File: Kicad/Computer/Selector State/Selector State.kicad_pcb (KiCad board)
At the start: 2 copper layers, 61 x 61 mm, 72 parts, among them IC1 FAN2558S38X, IC10 74LVC257AD,118, IC11 74LVC257AD,118, IC12 74LVC4245APW,118, IC13 MCP1802T-5002I_OT, IC2 74LVC32APW,118, IC3 74LVC32APW,118, IC4 74VHC595FT, IC5 74LVC2G08DP-Q100H, IC6 SN74ABT245BDBR, IC7 SN74ABT245BDBR, IC8 74ALVC04PW,118, IC9 74ALVC00PW,118, J1 Conn_01x02_Male, J10 Conn_01x02_Male, J11 Conn_01x10_Male, J12 Conn_01x02_Male, J2 Conn_01x12_Male, J3 Conn_01x02_Male, J4 Conn_01x02_Male, J5 Conn_01x12_Male, J6 Conn_01x02_Male, J7 Conn_01x02_Male, J8 Conn_01x10_Male, J9 Conn_01x02_Male

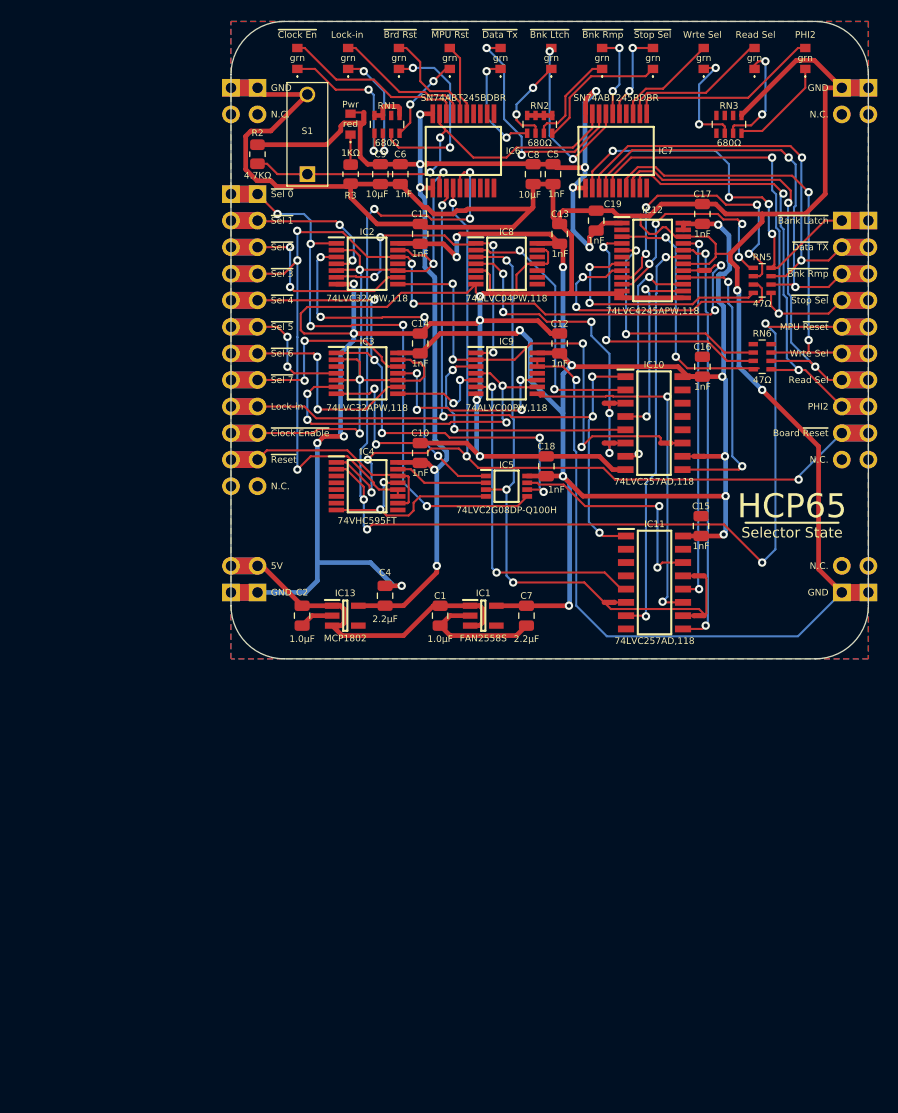
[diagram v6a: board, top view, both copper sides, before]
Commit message: Updated Selector State to reflect simulation changes.
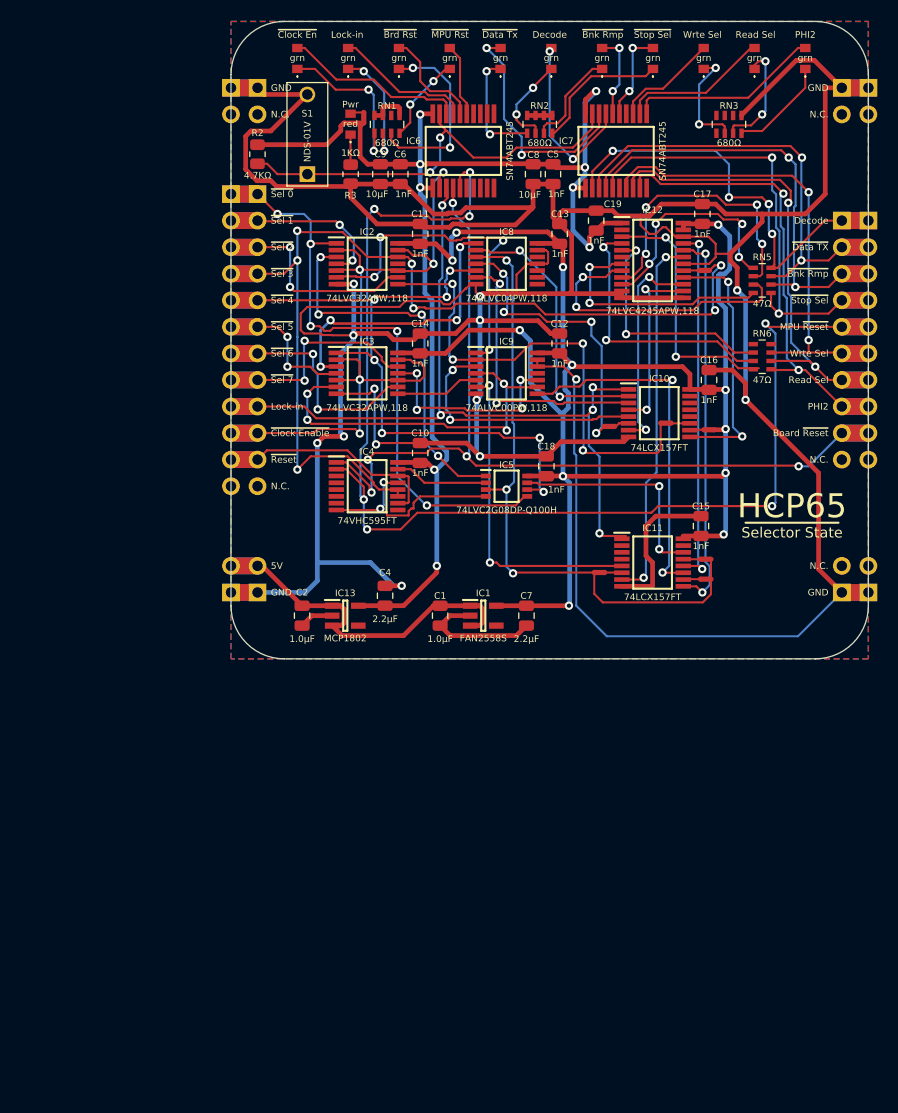
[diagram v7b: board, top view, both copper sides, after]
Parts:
- removed NT3: NetTie_2, NetTie:NetTie-2_SMD_Pad0.5mm
- IC10, IC11: value 74LVC257AD,118 -> 74LCX157FT; footprint SamacSys_Parts:SOIC127P600X175-16N -> SamacSys_Parts:SOP65P640X120-16N
- IC6, IC7: value SN74ABT245BDBR -> SN74ABT245
- moved NT8 3.55 mm to (187.6, 90.2)
- moved NT7 3.01 mm to (177.5, 89.5)
- moved NT4 2.71 mm to (188.0, 75.9)
- moved IC11 1.91 mm to (182.6, 88.6)
- moved NT1 1.91 mm to (183.8, 75.2)
- moved NT9 1.71 mm to (187.6, 88.3)
- moved NT5 1.59 mm to (178.4, 75.6)
- moved C16 1.42 mm to (188.0, 71.1)
- moved IC10 1.08 mm to (183.2, 74.3)
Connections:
- net /~{Bank Latch} renamed /Decode Done
- net /~{Bank Latch}_{1} renamed /Decode Done_{1}
- net /~{PHI2} Naked renamed /Select 0 ^{AND} Enable
- IC10 pad 3: /~{Bank Latch}_{2} -> /Decode Done_{2}
- IC3 pad 3: unconnected-(IC3-Pad3) -> /Select 4 ^{AND} Enable
- IC8 pad 1: /Select 1 ^{AND} Enable -> /Select 4 ^{AND} Enable
- IC8 pad 5: /GND -> /~{Select 4}
- IC8 pad 6: unconnected-(IC8-Pad6) -> /Decode Done_{2}
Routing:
- net /Select 4 ^{AND} Enable: track 0.00 -> 27.5 mm, vias 0 -> 4
- net /Decode Done_{2}: track 0.00 -> 26.7 mm, vias 0 -> 2
- net /GND: track 485.5 -> 503.5 mm
- net /~{Select 4}: track 55.8 -> 68.1 mm, vias 5 -> 7
- net /MPU ~{Reset}: track 128.0 -> 122.2 mm
- net Net-(IC10-Pad9): track 28.5 -> 24.8 mm
- net Net-(IC11-Pad7): track 38.7 -> 35.4 mm
- net Net-(IC8-Pad4): track 31.3 -> 28.0 mm, vias 5 -> 4
- net Net-(IC11-Pad9): track 40.3 -> 37.2 mm
- net /Select 2 ^{AND} Enable: track 44.2 -> 46.5 mm
- net /Select 6 ^{AND} Enable: track 9.88 -> 8.01 mm, vias 2 -> 0
- net Net-(IC10-Pad7): track 22.4 -> 20.7 mm
- net /Select 1 ^{AND} Enable: track 30.8 -> 32.3 mm
- net Net-(IC11-Pad12): track 36.1 -> 34.7 mm
- net /Board ~{Reset}: track 88.5 -> 87.4 mm
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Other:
- board text added: "Decode"
- board text removed: "~{Bank Latch}"
- board text removed: "~{Bnk Ltch}"

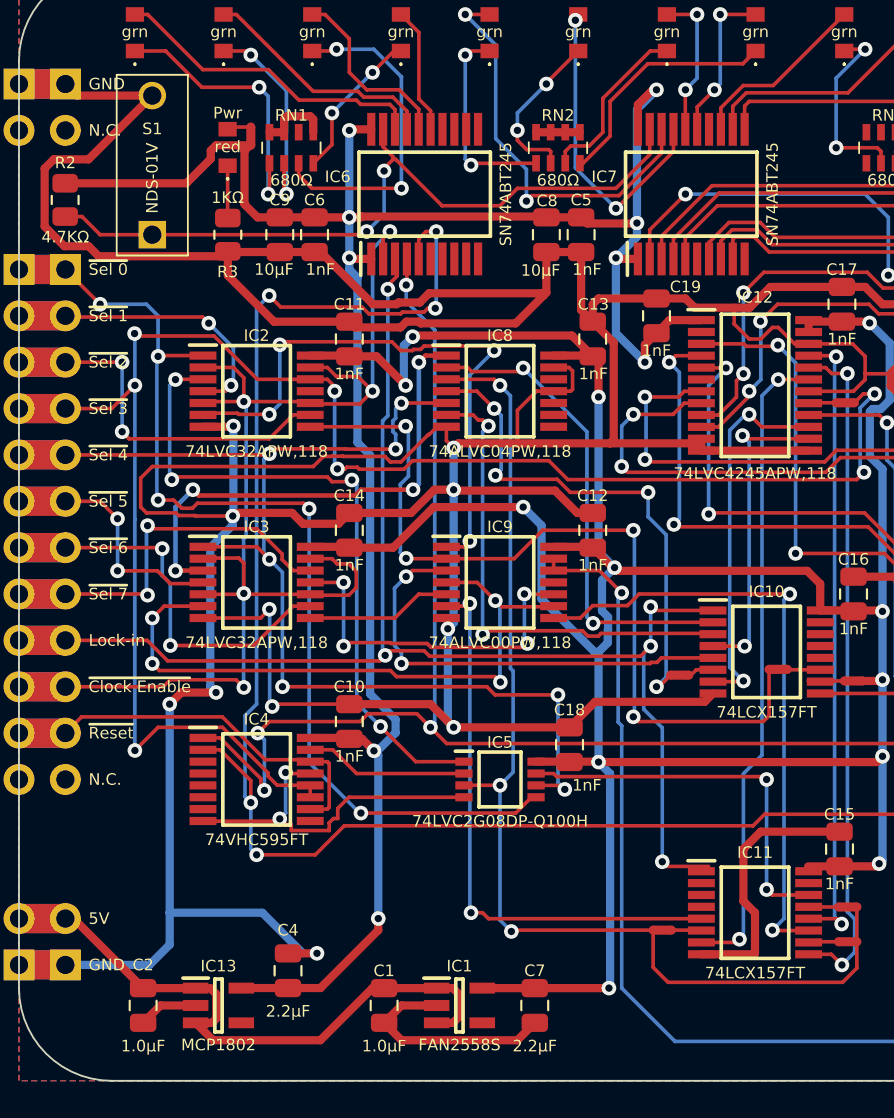
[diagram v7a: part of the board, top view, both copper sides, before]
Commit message: Added a 65C816 stress tester using a Raspberry Pi Pico.
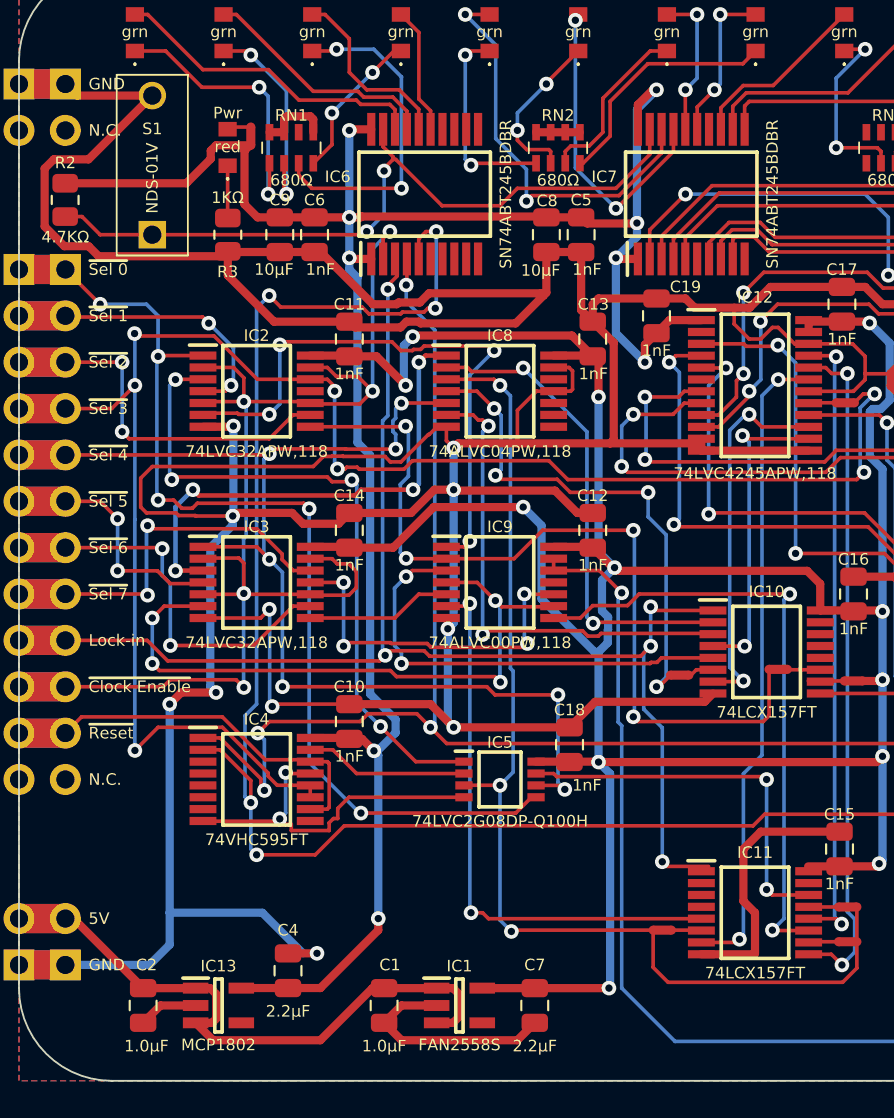
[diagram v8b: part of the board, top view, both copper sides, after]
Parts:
- C1, C2, C4, C7: value C_Small -> C_0805
- IC6, IC7: value SN74ABT245 -> SN74ABT245BDBR
- turned C1 to -90 degrees
- turned C2 to -90 degrees
- turned C4 to 90 degrees
- turned C7 to -90 degrees
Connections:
- C1 pad 1: /GND -> /Source 5V
- C1 pad 2: /Source 5V -> /GND
- C2 pad 1: /GND -> /Source 5V
- C2 pad 2: /Source 5V -> /GND
- C4 pad 1: /GND -> /5V
- C4 pad 2: /5V -> /GND
- C7 pad 1: /GND -> /3.8V
- C7 pad 2: /3.8V -> /GND
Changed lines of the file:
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@@
   )
   (footprint "Capacitor_SMD:C_0805_2012Metric" (layer "F.Cu")
-    (at 149.040978 93.6625 90)
+    (at 149.040978 93.6625 -90)
     (descr "Capacitor SMD 0805 (2012 Metric), square (rectangular) end terminal, IPC_7351 nominal, (Body size source: IPC-SM-782 page 76, https://www.pcb-3d.com/wordpress/wp-content/uploads/ipc-sm-782a_amendment_1_and_2.pdf, https://docs.google.com/spreadsheets/d/1BsfQQcO9C6DZCsRaXUlFlo91Tg2WpOkGARC1WS5S8t0/edit?usp=sharing), generated with kicad-footprint-generator")
     (tags "capacitor")
@@
     (property "Sheetname" "")
     (attr smd)
-    (fp_text reference "C2" (at 2.2225 0 180) (layer "F.SilkS")
-      (effects (font (size 0.635 0.635) (thickness 0.15)))
-    )
-    (fp_text value "C_Small" (at 0 1.68 90) (layer "F.Fab") hide
+    (fp_text reference "C2" (at -2.2225 -0.184022 180) (layer "F.SilkS")
+      (effects (font (size 0.635 0.635) (thickness 0.15)))
+    )
+    (fp_text value "C_0805" (at 0 1.68 90) (layer "F.Fab") hide
       (effects (font (size 1 1) (thickness 0.15)))
     )
-    (fp_text user "${Description}" (at -2.2225 0 unlocked) (layer "F.SilkS")
+    (fp_text user "${Description}" (at 2.2225 -0.184022 unlocked) (layer "F.SilkS")
       (effects (font (size 0.635 0.635) (thickness 0.15)))
     )
@@
     (fp_line (start 1 0.625) (end -1 0.625) (layer "F.Fab") (width 0.1))
     (fp_line (start -1 0.625) (end -1 -0.625) (layer "F.Fab") (width 0.1))
-    (pad "1" smd roundrect (at -0.95 0 90) (size 1 1.45) (layers "F.Cu" "F.Paste" "F.Mask") (roundrect_rratio 0.25)
+    (pad "1" smd roundrect (at -0.95 0 270) (size 1 1.45) (layers "F.Cu" "F.Paste" "F.Mask") (roundrect_rratio 0.25)
+      (net 1 "/Source 5V") (pintype "passive"))
+    (pad "2" smd roundrect (at 0.95 0 270) (size 1 1.45) (layers "F.Cu" "F.Paste" "F.Mask") (roundrect_rratio 0.25)
       (net 103 "/GND") (pintype "passive"))
-    (pad "2" smd roundrect (at 0.95 0 90) (size 1 1.45) (layers "F.Cu" "F.Paste" "F.Mask") (roundrect_rratio 0.25)
-      (net 1 "/Source 5V") (pintype "passive"))
     (model "${KICAD6_3DMODEL_DIR}/Capacitor_SMD.3dshapes/C_0805_2012Metric.wrl"
       (offset (xyz 0 0 0))
@@
       (effects (font (size 0.635 0.635) (thickness 0.15)))
     )
-    (fp_text value "SN74ABT245" (at 0 4.445 90) (layer "F.SilkS")
+    (fp_text value "SN74ABT245BDBR" (at 0 4.445 90) (layer "F.SilkS")
       (effects (font (size 0.635 0.635) (thickness 0.15)))
     )
@@
       (effects (font (size 0.635 0.635) (thickness 0.15)))
     )
-    (fp_text value "SN74ABT245" (at 0 4.445 90) (layer "F.SilkS")
+    (fp_text value "SN74ABT245BDBR" (at 0 4.445 90) (layer "F.SilkS")
       (effects (font (size 0.635 0.635) (thickness 0.15)))
     )
@@
   )
   (footprint "Capacitor_SMD:C_0805_2012Metric" (layer "F.Cu")
-    (at 156.978478 91.7575 -90)
+    (at 156.978478 91.7575 90)
     (descr "Capacitor SMD 0805 (2012 Metric), square (rectangular) end terminal, IPC_7351 nominal, (Body size source: IPC-SM-782 page 76, https://www.pcb-3d.com/wordpress/wp-content/uploads/ipc-sm-782a_amendment_1_and_2.pdf, https://docs.google.com/spreadsheets/d/1BsfQQcO9C6DZCsRaXUlFlo91Tg2WpOkGARC1WS5S8t0/edit?usp=sharing), generated with kicad-footprint-generator")
     (tags "capacitor")
@@
     (property "Sheetname" "")
     (attr smd)
-    (fp_text reference "C4" (at -2.2225 0 180) (layer "F.SilkS")
-      (effects (font (size 0.635 0.635) (thickness 0.15)))
-    )
-    (fp_text value "C_Small" (at 0 1.68 -270) (layer "F.Fab")
-      (effects (font (size 0.635 0.635) (thickness 0.15)))
-    )
-    (fp_text user "${Description}" (at 2.2225 0 unlocked) (layer "F.SilkS")
-      (effects (font (size 0.635 0.635) (thickness 0.15)))
-    )
-    (fp_text user "${REFERENCE}" (at 0 0 -270) (layer "F.Fab")
+    (fp_text reference "C4" (at 2.2225 0) (layer "F.SilkS")
+      (effects (font (size 0.635 0.635) (thickness 0.15)))
+    )
+    (fp_text value "C_0805" (at 0 1.68 90) (layer "F.Fab")
+      (effects (font (size 0.635 0.635) (thickness 0.15)))
+    )
+    (fp_text user "${Description}" (at -2.2225 0 unlocked) (layer "F.SilkS")
+      (effects (font (size 0.635 0.635) (thickness 0.15)))
+    )
+    (fp_text user "${REFERENCE}" (at 0 0 90) (layer "F.Fab")
       (effects (font (size 0.5 0.5) (thickness 0.08)))
     )
@@
     (fp_line (start -1 0.625) (end -1 -0.625) (layer "F.Fab") (width 0.1))
     (fp_line (start 1 0.625) (end -1 0.625) (layer "F.Fab") (width 0.1))
-    (pad "1" smd roundrect (at -0.95 0 270) (size 1 1.45) (layers "F.Cu" "F.Paste" "F.Mask") (roundrect_rratio 0.25)
+    (pad "1" smd roundrect (at -0.95 0 90) (size 1 1.45) (layers "F.Cu" "F.Paste" "F.Mask") (roundrect_rratio 0.25)
+      (net 104 "/5V") (pintype "passive"))
+    (pad "2" smd roundrect (at 0.95 0 90) (size 1 1.45) (layers "F.Cu" "F.Paste" "F.Mask") (roundrect_rratio 0.25)
       (net 103 "/GND") (pintype "passive"))
-    (pad "2" smd roundrect (at 0.95 0 270) (size 1 1.45) (layers "F.Cu" "F.Paste" "F.Mask") (roundrect_rratio 0.25)
-      (net 104 "/5V") (pintype "passive"))
     (model "${KICAD6_3DMODEL_DIR}/Capacitor_SMD.3dshapes/C_0805_2012Metric.wrl"
       (offset (xyz 0 0 0))
@@
   )
   (footprint "Capacitor_SMD:C_0805_2012Metric" (layer "F.Cu")
-    (at 162.2425 93.6625 90)
+    (at 162.2425 93.6625 -90)
     (descr "Capacitor SMD 0805 (2012 Metric), square (rectangular) end terminal, IPC_7351 nominal, (Body size source: IPC-SM-782 page 76, https://www.pcb-3d.com/wordpress/wp-content/uploads/ipc-sm-782a_amendment_1_and_2.pdf, https://docs.google.com/spreadsheets/d/1BsfQQcO9C6DZCsRaXUlFlo91Tg2WpOkGARC1WS5S8t0/edit?usp=sharing), generated with kicad-footprint-generator")
     (tags "capacitor")
@@
     (property "Sheetname" "")
     (attr smd)
-    (fp_text reference "C1" (at 1.9025 0 180) (layer "F.SilkS")
-      (effects (font (size 0.635 0.635) (thickness 0.15)))
-    )
-    (fp_text value "C_Small" (at 0 1.68 90) (layer "F.Fab")
-      (effects (font (size 0.635 0.635) (thickness 0.15)))
-    )
-    (fp_text user "${Description}" (at -2.2225 0 unlocked) (layer "F.SilkS")
+    (fp_text reference "C1" (at -2.2225 -0.3175) (layer "F.SilkS")
+      (effects (font (size 0.635 0.635) (thickness 0.15)))
+    )
+    (fp_text value "C_0805" (at 0 1.68 90) (layer "F.Fab")
+      (effects (font (size 0.635 0.635) (thickness 0.15)))
+    )
+    (fp_text user "${Description}" (at 2.2225 0 unlocked) (layer "F.SilkS")
       (effects (font (size 0.635 0.635) (thickness 0.15)))
     )
@@
     (fp_line (start 1 -0.625) (end 1 0.625) (layer "F.Fab") (width 0.1))
     (fp_line (start 1 0.625) (end -1 0.625) (layer "F.Fab") (width 0.1))
-    (pad "1" smd roundrect (at -0.95 0 90) (size 1 1.45) (layers "F.Cu" "F.Paste" "F.Mask") (roundrect_rratio 0.25)
+    (pad "1" smd roundrect (at -0.95 0 270) (size 1 1.45) (layers "F.Cu" "F.Paste" "F.Mask") (roundrect_rratio 0.25)
+      (net 1 "/Source 5V") (pintype "passive"))
+    (pad "2" smd roundrect (at 0.95 0 270) (size 1 1.45) (layers "F.Cu" "F.Paste" "F.Mask") (roundrect_rratio 0.25)
       (net 103 "/GND") (pintype "passive"))
-    (pad "2" smd roundrect (at 0.95 0 90) (size 1 1.45) (layers "F.Cu" "F.Paste" "F.Mask") (roundrect_rratio 0.25)
-      (net 1 "/Source 5V") (pintype "passive"))
     (model "${KICAD6_3DMODEL_DIR}/Capacitor_SMD.3dshapes/C_0805_2012Metric.wrl"
       (offset (xyz 0 0 0))
@@
   )
   (footprint "Capacitor_SMD:C_0805_2012Metric" (layer "F.Cu")
-    (at 170.4975 93.6625 90)
+    (at 170.4975 93.6625 -90)
     (descr "Capacitor SMD 0805 (2012 Metric), square (rectangular) end terminal, IPC_7351 nominal, (Body size source: IPC-SM-782 page 76, https://www.pcb-3d.com/wordpress/wp-content/uploads/ipc-sm-782a_amendment_1_and_2.pdf, https://docs.google.com/spreadsheets/d/1BsfQQcO9C6DZCsRaXUlFlo91Tg2WpOkGARC1WS5S8t0/edit?usp=sharing), generated with kicad-footprint-generator")
     (tags "capacitor")
@@
     (property "Sheetname" "")
     (attr smd)
-    (fp_text reference "C7" (at 1.905 0 180) (layer "F.SilkS")
-      (effects (font (size 0.635 0.635) (thickness 0.15)))
-    )
-    (fp_text value "C_Small" (at 0 1.68 90) (layer "F.Fab")
-      (effects (font (size 0.635 0.635) (thickness 0.15)))
-    )
-    (fp_text user "${Description}" (at -2.2225 0 unlocked) (layer "F.SilkS")
+    (fp_text reference "C7" (at -2.2225 0) (layer "F.SilkS")
+      (effects (font (size 0.635 0.635) (thickness 0.15)))
+    )
+    (fp_text value "C_0805" (at 0 1.68 90) (layer "F.Fab")
+      (effects (font (size 0.635 0.635) (thickness 0.15)))
+    )
+    (fp_text user "${Description}" (at 2.2225 0 unlocked) (layer "F.SilkS")
       (effects (font (size 0.635 0.635) (thickness 0.15)))
     )
@@
     (fp_line (start 1 0.625) (end -1 0.625) (layer "F.Fab") (width 0.1))
     (fp_line (start -1 0.625) (end -1 -0.625) (layer "F.Fab") (width 0.1))
-    (pad "1" smd roundrect (at -0.95 0 90) (size 1 1.45) (layers "F.Cu" "F.Paste" "F.Mask") (roundrect_rratio 0.25)
+    (pad "1" smd roundrect (at -0.95 0 270) (size 1 1.45) (layers "F.Cu" "F.Paste" "F.Mask") (roundrect_rratio 0.25)
+      (net 105 "/3.8V") (pintype "passive"))
+    (pad "2" smd roundrect (at 0.95 0 270) (size 1 1.45) (layers "F.Cu" "F.Paste" "F.Mask") (roundrect_rratio 0.25)
       (net 103 "/GND") (pintype "passive"))
-    (pad "2" smd roundrect (at 0.95 0 90) (size 1 1.45) (layers "F.Cu" "F.Paste" "F.Mask") (roundrect_rratio 0.25)
-      (net 105 "/3.8V") (pintype "passive"))
     (model "${KICAD6_3DMODEL_DIR}/Capacitor_SMD.3dshapes/C_0805_2012Metric.wrl"
       (offset (xyz 0 0 0))
